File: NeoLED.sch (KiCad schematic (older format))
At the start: 2 parts

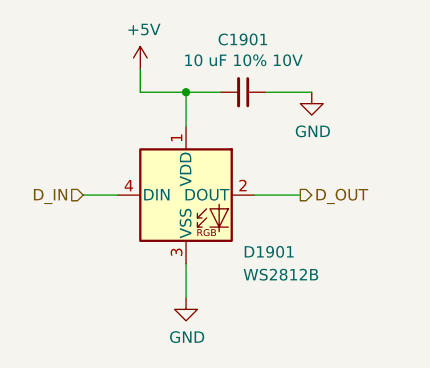
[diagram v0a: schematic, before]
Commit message: Added PCA9745B16B. Updated schematic. ERC Passes.
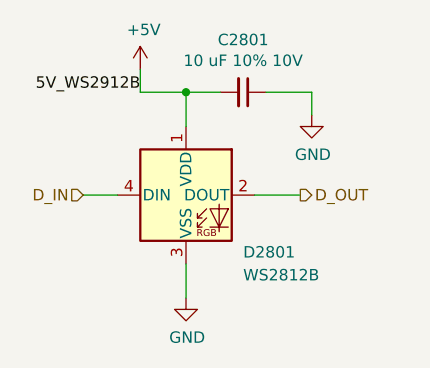
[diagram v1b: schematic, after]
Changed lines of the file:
@@
 AR Path="/61A0B661/61A1D841/61A17A93" Ref="D2701"  Part="1"
 AR Path="/61A0B661/61A1D845/61A17A93" Ref="D2801"  Part="1"
-F 0 "D1901" H 5450 2450 50  0000 L CNN
+F 0 "D2801" H 5450 2450 50  0000 L CNN
 F 1 "WS2812B" H 5450 2350 50  0000 L CNN
 F 2 "LED_SMD:LED_WS2812B_PLCC4_5.0x5.0mm_P3.2mm" H 5250 2400 50  0001 L TNN
@@
 AR Path="/61A0B661/61A1D841/61A18EF9" Ref="#PWR02701"  Part="1"
 AR Path="/61A0B661/61A1D845/61A18EF9" Ref="#PWR02801"  Part="1"
-F 0 "#PWR01901" H 5000 2000 50  0001 C CNN
+F 0 "#PWR02801" H 5000 2000 50  0001 C CNN
 F 1 "+5V" H 5015 2323 50  0000 C CNN
 F 2 "" H 5000 2150 50  0001 C CNN
@@
 AR Path="/61A0B661/61A1D841/61A198EA" Ref="C2701"  Part="1"
 AR Path="/61A0B661/61A1D845/61A198EA" Ref="C2801"  Part="1"
-F 0 "C1901" V 5221 2250 50  0000 C CNN
+F 0 "C2801" V 5221 2250 50  0000 C CNN
 F 1 "10 uF 10% 10V" V 5312 2250 50  0000 C CNN
 F 2 "Capacitor_SMD:C_0805_2012Metric_Pad1.18x1.45mm_HandSolder" H 5450 2250 50  0001 C CNN
@@
 AR Path="/61A0B661/61A1D841/61A1B1AB" Ref="#PWR02702"  Part="1"
 AR Path="/61A0B661/61A1D845/61A1B1AB" Ref="#PWR02802"  Part="1"
-F 0 "#PWR01902" H 5200 2900 50  0001 C CNN
+F 0 "#PWR02802" H 5200 2900 50  0001 C CNN
 F 1 "GND" H 5205 2977 50  0000 C CNN
 F 2 "" H 5200 3150 50  0001 C CNN
@@
 L power:GND #PWR01903
 U 1 1 61A1B656
-P 5750 2250
+P 5750 2350
 AR Path="/61A0B661/61A171D3/61A1B656" Ref="#PWR01903"  Part="1"
 AR Path="/61A0B661/61A1CCBC/61A1B656" Ref="#PWR02003"  Part="1"
@@
 AR Path="/61A0B661/61A1D841/61A1B656" Ref="#PWR02703"  Part="1"
 AR Path="/61A0B661/61A1D845/61A1B656" Ref="#PWR02803"  Part="1"
-F 0 "#PWR01903" H 5750 2000 50  0001 C CNN
-F 1 "GND" H 5755 2077 50  0000 C CNN
-F 2 "" H 5750 2250 50  0001 C CNN
-F 3 "" H 5750 2250 50  0001 C CNN
-	1    5750 2250
+F 0 "#PWR02803" H 5750 2100 50  0001 C CNN
+F 1 "GND" H 5755 2177 50  0000 C CNN
+F 2 "" H 5750 2350 50  0001 C CNN
+F 3 "" H 5750 2350 50  0001 C CNN
+	1    5750 2350
 	1    0    0    -1
 $EndComp
@@
 	5000 2250 5000 2150
 Connection ~ 5200 2250
+Text Label 5000 2250 2    50   ~ 0
+5V_WS2912B
+Wire Wire Line
+	5750 2250 5750 2350
 $EndSCHEMATC

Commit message: fixed broken schematics becuase of deleted rescue files. ECA passes.
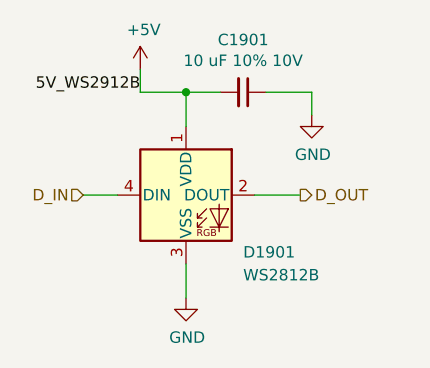
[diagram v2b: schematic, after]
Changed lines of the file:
@@
 AR Path="/61A0B661/61A1D841/61A17A93" Ref="D2701"  Part="1"
 AR Path="/61A0B661/61A1D845/61A17A93" Ref="D2801"  Part="1"
-F 0 "D2801" H 5450 2450 50  0000 L CNN
+F 0 "D1901" H 5450 2450 50  0000 L CNN
 F 1 "WS2812B" H 5450 2350 50  0000 L CNN
 F 2 "LED_SMD:LED_WS2812B_PLCC4_5.0x5.0mm_P3.2mm" H 5250 2400 50  0001 L TNN
@@
 AR Path="/61A0B661/61A1D841/61A198EA" Ref="C2701"  Part="1"
 AR Path="/61A0B661/61A1D845/61A198EA" Ref="C2801"  Part="1"
-F 0 "C2801" V 5221 2250 50  0000 C CNN
+F 0 "C1901" V 5221 2250 50  0000 C CNN
 F 1 "10 uF 10% 10V" V 5312 2250 50  0000 C CNN
 F 2 "Capacitor_SMD:C_0805_2012Metric_Pad1.18x1.45mm_HandSolder" H 5450 2250 50  0001 C CNN

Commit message: initial layout
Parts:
- renumbered C1901 to C1701, D1901 to D1701
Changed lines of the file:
@@
 $Descr A4 11693 8268
 encoding utf-8
-Sheet 17 29
+Sheet 18 29
 Title ""
 Date ""
@@
 $EndDescr
 $Comp
-L TMPCB_R2:WS2812B D1901
+L TMPCB_R2:WS2812B D1701
 U 1 1 61A17A93
 P 5200 2700
-AR Path="/61A0B661/61A171D3/61A17A93" Ref="D1901"  Part="1"
-AR Path="/61A0B661/61A1CCBC/61A17A93" Ref="D2001"  Part="1"
-AR Path="/61A0B661/61A1CE5F/61A17A93" Ref="D2101"  Part="1"
-AR Path="/61A0B661/61A1D175/61A17A93" Ref="D2201"  Part="1"
-AR Path="/61A0B661/61A1D179/61A17A93" Ref="D2301"  Part="1"
-AR Path="/61A0B661/61A1D17D/61A17A93" Ref="D2401"  Part="1"
-AR Path="/61A0B661/61A1D839/61A17A93" Ref="D2501"  Part="1"
-AR Path="/61A0B661/61A1D83D/61A17A93" Ref="D2601"  Part="1"
-AR Path="/61A0B661/61A1D841/61A17A93" Ref="D2701"  Part="1"
-AR Path="/61A0B661/61A1D845/61A17A93" Ref="D2801"  Part="1"
-F 0 "D1901" H 5450 2450 50  0000 L CNN
+AR Path="/61A0B661/61A171D3/61A17A93" Ref="D1701"  Part="1"
+AR Path="/61A0B661/61A1CCBC/61A17A93" Ref="D1801"  Part="1"
+AR Path="/61A0B661/61A1CE5F/61A17A93" Ref="D1901"  Part="1"
+AR Path="/61A0B661/61A1D175/61A17A93" Ref="D2001"  Part="1"
+AR Path="/61A0B661/61A1D179/61A17A93" Ref="D2101"  Part="1"
+AR Path="/61A0B661/61A1D17D/61A17A93" Ref="D2201"  Part="1"
+AR Path="/61A0B661/61A1D839/61A17A93" Ref="D2301"  Part="1"
+AR Path="/61A0B661/61A1D83D/61A17A93" Ref="D2401"  Part="1"
+AR Path="/61A0B661/61A1D841/61A17A93" Ref="D2501"  Part="1"
+AR Path="/61A0B661/61A1D845/61A17A93" Ref="D2601"  Part="1"
+F 0 "D1801" H 5450 2450 50  0000 L CNN
 F 1 "WS2812B" H 5450 2350 50  0000 L CNN
 F 2 "LED_SMD:LED_WS2812B_PLCC4_5.0x5.0mm_P3.2mm" H 5250 2400 50  0001 L TNN
@@
 	5200 3150 5200 3000
 $Comp
-L power:+5V #PWR01901
+L power:+5V #PWR01701
 U 1 1 61A18EF9
 P 5000 2150
-AR Path="/61A0B661/61A171D3/61A18EF9" Ref="#PWR01901"  Part="1"
-AR Path="/61A0B661/61A1CCBC/61A18EF9" Ref="#PWR02001"  Part="1"
-AR Path="/61A0B661/61A1CE5F/61A18EF9" Ref="#PWR02101"  Part="1"
-AR Path="/61A0B661/61A1D175/61A18EF9" Ref="#PWR02201"  Part="1"
-AR Path="/61A0B661/61A1D179/61A18EF9" Ref="#PWR02301"  Part="1"
-AR Path="/61A0B661/61A1D17D/61A18EF9" Ref="#PWR02401"  Part="1"
-AR Path="/61A0B661/61A1D839/61A18EF9" Ref="#PWR02501"  Part="1"
-AR Path="/61A0B661/61A1D83D/61A18EF9" Ref="#PWR02601"  Part="1"
-AR Path="/61A0B661/61A1D841/61A18EF9" Ref="#PWR02701"  Part="1"
-AR Path="/61A0B661/61A1D845/61A18EF9" Ref="#PWR02801"  Part="1"
-F 0 "#PWR02801" H 5000 2000 50  0001 C CNN
+AR Path="/61A0B661/61A171D3/61A18EF9" Ref="#PWR01701"  Part="1"
+AR Path="/61A0B661/61A1CCBC/61A18EF9" Ref="#PWR01801"  Part="1"
+AR Path="/61A0B661/61A1CE5F/61A18EF9" Ref="#PWR01901"  Part="1"
+AR Path="/61A0B661/61A1D175/61A18EF9" Ref="#PWR02001"  Part="1"
+AR Path="/61A0B661/61A1D179/61A18EF9" Ref="#PWR02101"  Part="1"
+AR Path="/61A0B661/61A1D17D/61A18EF9" Ref="#PWR02201"  Part="1"
+AR Path="/61A0B661/61A1D839/61A18EF9" Ref="#PWR02301"  Part="1"
+AR Path="/61A0B661/61A1D83D/61A18EF9" Ref="#PWR02401"  Part="1"
+AR Path="/61A0B661/61A1D841/61A18EF9" Ref="#PWR02501"  Part="1"
+AR Path="/61A0B661/61A1D845/61A18EF9" Ref="#PWR02601"  Part="1"
+F 0 "#PWR01801" H 5000 2000 50  0001 C CNN
 F 1 "+5V" H 5015 2323 50  0000 C CNN
 F 2 "" H 5000 2150 50  0001 C CNN
@@
 $EndComp
 $Comp
-L Device:C_Small C1901
+L Device:C_Small C1701
 U 1 1 61A198EA
 P 5450 2250
-AR Path="/61A0B661/61A171D3/61A198EA" Ref="C1901"  Part="1"
-AR Path="/61A0B661/61A1CCBC/61A198EA" Ref="C2001"  Part="1"
-AR Path="/61A0B661/61A1CE5F/61A198EA" Ref="C2101"  Part="1"
-AR Path="/61A0B661/61A1D175/61A198EA" Ref="C2201"  Part="1"
-AR Path="/61A0B661/61A1D179/61A198EA" Ref="C2301"  Part="1"
-AR Path="/61A0B661/61A1D17D/61A198EA" Ref="C2401"  Part="1"
-AR Path="/61A0B661/61A1D839/61A198EA" Ref="C2501"  Part="1"
-AR Path="/61A0B661/61A1D83D/61A198EA" Ref="C2601"  Part="1"
-AR Path="/61A0B661/61A1D841/61A198EA" Ref="C2701"  Part="1"
-AR Path="/61A0B661/61A1D845/61A198EA" Ref="C2801"  Part="1"
-F 0 "C1901" V 5221 2250 50  0000 C CNN
+AR Path="/61A0B661/61A171D3/61A198EA" Ref="C1701"  Part="1"
+AR Path="/61A0B661/61A1CCBC/61A198EA" Ref="C1801"  Part="1"
+AR Path="/61A0B661/61A1CE5F/61A198EA" Ref="C1901"  Part="1"
+AR Path="/61A0B661/61A1D175/61A198EA" Ref="C2001"  Part="1"
+AR Path="/61A0B661/61A1D179/61A198EA" Ref="C2101"  Part="1"
+AR Path="/61A0B661/61A1D17D/61A198EA" Ref="C2201"  Part="1"
+AR Path="/61A0B661/61A1D839/61A198EA" Ref="C2301"  Part="1"
+AR Path="/61A0B661/61A1D83D/61A198EA" Ref="C2401"  Part="1"
+AR Path="/61A0B661/61A1D841/61A198EA" Ref="C2501"  Part="1"
+AR Path="/61A0B661/61A1D845/61A198EA" Ref="C2601"  Part="1"
+F 0 "C1801" V 5221 2250 50  0000 C CNN
 F 1 "10 uF 10% 10V" V 5312 2250 50  0000 C CNN
 F 2 "Capacitor_SMD:C_0805_2012Metric_Pad1.18x1.45mm_HandSolder" H 5450 2250 50  0001 C CNN
@@
 $EndComp
 $Comp
-L power:GND #PWR01902
+L power:GND #PWR01702
 U 1 1 61A1B1AB
 P 5200 3150
-AR Path="/61A0B661/61A171D3/61A1B1AB" Ref="#PWR01902"  Part="1"
-AR Path="/61A0B661/61A1CCBC/61A1B1AB" Ref="#PWR02002"  Part="1"
-AR Path="/61A0B661/61A1CE5F/61A1B1AB" Ref="#PWR02102"  Part="1"
-AR Path="/61A0B661/61A1D175/61A1B1AB" Ref="#PWR02202"  Part="1"
-AR Path="/61A0B661/61A1D179/61A1B1AB" Ref="#PWR02302"  Part="1"
-AR Path="/61A0B661/61A1D17D/61A1B1AB" Ref="#PWR02402"  Part="1"
-AR Path="/61A0B661/61A1D839/61A1B1AB" Ref="#PWR02502"  Part="1"
-AR Path="/61A0B661/61A1D83D/61A1B1AB" Ref="#PWR02602"  Part="1"
-AR Path="/61A0B661/61A1D841/61A1B1AB" Ref="#PWR02702"  Part="1"
-AR Path="/61A0B661/61A1D845/61A1B1AB" Ref="#PWR02802"  Part="1"
-F 0 "#PWR02802" H 5200 2900 50  0001 C CNN
+AR Path="/61A0B661/61A171D3/61A1B1AB" Ref="#PWR01702"  Part="1"
+AR Path="/61A0B661/61A1CCBC/61A1B1AB" Ref="#PWR01802"  Part="1"
+AR Path="/61A0B661/61A1CE5F/61A1B1AB" Ref="#PWR01902"  Part="1"
+AR Path="/61A0B661/61A1D175/61A1B1AB" Ref="#PWR02002"  Part="1"
+AR Path="/61A0B661/61A1D179/61A1B1AB" Ref="#PWR02102"  Part="1"
+AR Path="/61A0B661/61A1D17D/61A1B1AB" Ref="#PWR02202"  Part="1"
+AR Path="/61A0B661/61A1D839/61A1B1AB" Ref="#PWR02302"  Part="1"
+AR Path="/61A0B661/61A1D83D/61A1B1AB" Ref="#PWR02402"  Part="1"
+AR Path="/61A0B661/61A1D841/61A1B1AB" Ref="#PWR02502"  Part="1"
+AR Path="/61A0B661/61A1D845/61A1B1AB" Ref="#PWR02602"  Part="1"
+F 0 "#PWR01802" H 5200 2900 50  0001 C CNN
 F 1 "GND" H 5205 2977 50  0000 C CNN
 F 2 "" H 5200 3150 50  0001 C CNN
@@
 $EndComp
 $Comp
-L power:GND #PWR01903
+L power:GND #PWR01703
 U 1 1 61A1B656
 P 5750 2350
-AR Path="/61A0B661/61A171D3/61A1B656" Ref="#PWR01903"  Part="1"
-AR Path="/61A0B661/61A1CCBC/61A1B656" Ref="#PWR02003"  Part="1"
-AR Path="/61A0B661/61A1CE5F/61A1B656" Ref="#PWR02103"  Part="1"
-AR Path="/61A0B661/61A1D175/61A1B656" Ref="#PWR02203"  Part="1"
-AR Path="/61A0B661/61A1D179/61A1B656" Ref="#PWR02303"  Part="1"
-AR Path="/61A0B661/61A1D17D/61A1B656" Ref="#PWR02403"  Part="1"
-AR Path="/61A0B661/61A1D839/61A1B656" Ref="#PWR02503"  Part="1"
-AR Path="/61A0B661/61A1D83D/61A1B656" Ref="#PWR02603"  Part="1"
-AR Path="/61A0B661/61A1D841/61A1B656" Ref="#PWR02703"  Part="1"
-AR Path="/61A0B661/61A1D845/61A1B656" Ref="#PWR02803"  Part="1"
-F 0 "#PWR02803" H 5750 2100 50  0001 C CNN
+AR Path="/61A0B661/61A171D3/61A1B656" Ref="#PWR01703"  Part="1"
+AR Path="/61A0B661/61A1CCBC/61A1B656" Ref="#PWR01803"  Part="1"
+AR Path="/61A0B661/61A1CE5F/61A1B656" Ref="#PWR01903"  Part="1"
+AR Path="/61A0B661/61A1D175/61A1B656" Ref="#PWR02003"  Part="1"
+AR Path="/61A0B661/61A1D179/61A1B656" Ref="#PWR02103"  Part="1"
+AR Path="/61A0B661/61A1D17D/61A1B656" Ref="#PWR02203"  Part="1"
+AR Path="/61A0B661/61A1D839/61A1B656" Ref="#PWR02303"  Part="1"
+AR Path="/61A0B661/61A1D83D/61A1B656" Ref="#PWR02403"  Part="1"
+AR Path="/61A0B661/61A1D841/61A1B656" Ref="#PWR02503"  Part="1"
+AR Path="/61A0B661/61A1D845/61A1B656" Ref="#PWR02603"  Part="1"
+F 0 "#PWR01803" H 5750 2100 50  0001 C CNN
 F 1 "GND" H 5755 2177 50  0000 C CNN
 F 2 "" H 5750 2350 50  0001 C CNN

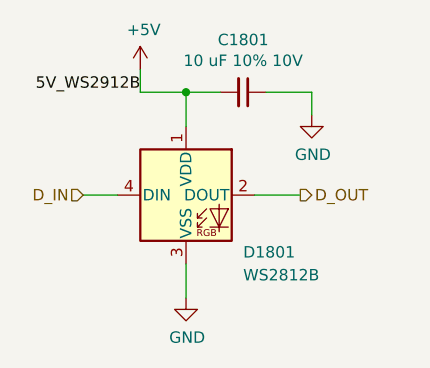
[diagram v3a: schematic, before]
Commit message: Switch NeoPixel to SK6812MINI-E
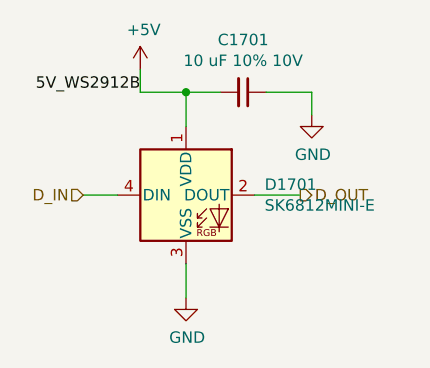
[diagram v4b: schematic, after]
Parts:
- removed D1701: WS2812B, LED_SMD:LED_WS2812B_PLCC4_5.0x5.0mm_P3.2mm, symbol TMPCB_R2:WS2812B
- added D1701: SK6812MINI-E, Macro Keyboard:MX_SK6812MINI-E, symbol Macro_Keyboard:SK6812MINI-E
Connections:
- net +5V: now also D1701.1 (VDD)
- net D_IN: now also D1701.4 (DIN)
- net D_OUT: now also D1701.2 (DOUT)
- net GND: now also D1701.3 (VSS)
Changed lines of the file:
@@
 $Descr A4 11693 8268
 encoding utf-8
-Sheet 18 29
+Sheet 17 29
 Title ""
 Date ""
@@
 Comment4 ""
 $EndDescr
-$Comp
-L TMPCB_R2:WS2812B D1701
-U 1 1 61A17A93
-P 5200 2700
-AR Path="/61A0B661/61A171D3/61A17A93" Ref="D1701"  Part="1"
-AR Path="/61A0B661/61A1CCBC/61A17A93" Ref="D1801"  Part="1"
-AR Path="/61A0B661/61A1CE5F/61A17A93" Ref="D1901"  Part="1"
-AR Path="/61A0B661/61A1D175/61A17A93" Ref="D2001"  Part="1"
-AR Path="/61A0B661/61A1D179/61A17A93" Ref="D2101"  Part="1"
-AR Path="/61A0B661/61A1D17D/61A17A93" Ref="D2201"  Part="1"
-AR Path="/61A0B661/61A1D839/61A17A93" Ref="D2301"  Part="1"
-AR Path="/61A0B661/61A1D83D/61A17A93" Ref="D2401"  Part="1"
-AR Path="/61A0B661/61A1D841/61A17A93" Ref="D2501"  Part="1"
-AR Path="/61A0B661/61A1D845/61A17A93" Ref="D2601"  Part="1"
-F 0 "D1801" H 5450 2450 50  0000 L CNN
-F 1 "WS2812B" H 5450 2350 50  0000 L CNN
-F 2 "LED_SMD:LED_WS2812B_PLCC4_5.0x5.0mm_P3.2mm" H 5250 2400 50  0001 L TNN
-F 3 "http://cdn.sparkfun.com/datasheets/BreakoutBoards/WS2812B.pdf" H 5300 2325 50  0001 L TNN
-F 4 "1568-COM-16347CT-ND" H 5200 2700 50  0001 C CNN "Digikey PN"
-F 5 "SparkFun Electronics" H 5200 2700 50  0001 C CNN "MFG"
-F 6 "COM-16347" H 5200 2700 50  0001 C CNN "MFG #"
-	1    5200 2700
-	1    0    0    -1
-$EndComp
 Text HLabel 4750 2700 0    50   Input ~ 0
 D_IN
@@
 AR Path="/61A0B661/61A1D841/61A18EF9" Ref="#PWR02501"  Part="1"
 AR Path="/61A0B661/61A1D845/61A18EF9" Ref="#PWR02601"  Part="1"
-F 0 "#PWR01801" H 5000 2000 50  0001 C CNN
+F 0 "#PWR01701" H 5000 2000 50  0001 C CNN
 F 1 "+5V" H 5015 2323 50  0000 C CNN
 F 2 "" H 5000 2150 50  0001 C CNN
@@
 AR Path="/61A0B661/61A1D841/61A198EA" Ref="C2501"  Part="1"
 AR Path="/61A0B661/61A1D845/61A198EA" Ref="C2601"  Part="1"
-F 0 "C1801" V 5221 2250 50  0000 C CNN
+F 0 "C1701" V 5221 2250 50  0000 C CNN
 F 1 "10 uF 10% 10V" V 5312 2250 50  0000 C CNN
 F 2 "Capacitor_SMD:C_0805_2012Metric_Pad1.18x1.45mm_HandSolder" H 5450 2250 50  0001 C CNN
@@
 AR Path="/61A0B661/61A1D841/61A1B1AB" Ref="#PWR02502"  Part="1"
 AR Path="/61A0B661/61A1D845/61A1B1AB" Ref="#PWR02602"  Part="1"
-F 0 "#PWR01802" H 5200 2900 50  0001 C CNN
+F 0 "#PWR01702" H 5200 2900 50  0001 C CNN
 F 1 "GND" H 5205 2977 50  0000 C CNN
 F 2 "" H 5200 3150 50  0001 C CNN
@@
 AR Path="/61A0B661/61A1D841/61A1B656" Ref="#PWR02503"  Part="1"
 AR Path="/61A0B661/61A1D845/61A1B656" Ref="#PWR02603"  Part="1"
-F 0 "#PWR01803" H 5750 2100 50  0001 C CNN
+F 0 "#PWR01703" H 5750 2100 50  0001 C CNN
 F 1 "GND" H 5755 2177 50  0000 C CNN
 F 2 "" H 5750 2350 50  0001 C CNN
@@
 Wire Wire Line
 	5750 2250 5750 2350
+$Comp
+L Macro_Keyboard:SK6812MINI-E D1701
+U 1 1 61A46C26
+P 5200 2700
+AR Path="/61A0B661/61A171D3/61A46C26" Ref="D1701"  Part="1"
+AR Path="/61A0B661/61A1CCBC/61A46C26" Ref="D1801"  Part="1"
+AR Path="/61A0B661/61A1CE5F/61A46C26" Ref="D1901"  Part="1"
+AR Path="/61A0B661/61A1D175/61A46C26" Ref="D2001"  Part="1"
+AR Path="/61A0B661/61A1D179/61A46C26" Ref="D2101"  Part="1"
+AR Path="/61A0B661/61A1D17D/61A46C26" Ref="D2201"  Part="1"
+AR Path="/61A0B661/61A1D839/61A46C26" Ref="D2301"  Part="1"
+AR Path="/61A0B661/61A1D83D/61A46C26" Ref="D2401"  Part="1"
+AR Path="/61A0B661/61A1D841/61A46C26" Ref="D2501"  Part="1"
+AR Path="/61A0B661/61A1D845/61A46C26" Ref="D2601"  Part="1"
+F 0 "D1701" H 5544 2746 50  0000 L CNN
+F 1 "SK6812MINI-E" H 5544 2655 50  0000 L CNN
+F 2 "Macro Keyboard:MX_SK6812MINI-E" H 5250 2400 50  0001 L TNN
+F 3 "https://cdn-shop.adafruit.com/product-files/4960/4960_SK6812MINI-E_REV02_EN.pdf" H 5300 2325 50  0001 L TNN
+F 4 "1528-4960-ND" H 5200 2700 50  0001 C CNN "Digikey PN"
+F 5 "Adafruit Industries LLC" H 5200 2700 50  0001 C CNN "MFG"
+F 6 "4960" H 5200 2700 50  0001 C CNN "MFG #"
+	1    5200 2700
+	1    0    0    -1
+$EndComp
 $EndSCHEMATC

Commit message: Starting routing
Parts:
- D1701: footprint Macro Keyboard:MX_SK6812MINI-E -> Macro Keyboard:MX_SK6812MINI-E_REV
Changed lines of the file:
@@
 $Descr A4 11693 8268
 encoding utf-8
-Sheet 17 29
+Sheet 18 30
 Title ""
 Date ""
@@
 AR Path="/61A0B661/61A1D841/61A18EF9" Ref="#PWR02501"  Part="1"
 AR Path="/61A0B661/61A1D845/61A18EF9" Ref="#PWR02601"  Part="1"
-F 0 "#PWR01701" H 5000 2000 50  0001 C CNN
+F 0 "#PWR01801" H 5000 2000 50  0001 C CNN
 F 1 "+5V" H 5015 2323 50  0000 C CNN
 F 2 "" H 5000 2150 50  0001 C CNN
@@
 AR Path="/61A0B661/61A1D841/61A198EA" Ref="C2501"  Part="1"
 AR Path="/61A0B661/61A1D845/61A198EA" Ref="C2601"  Part="1"
-F 0 "C1701" V 5221 2250 50  0000 C CNN
+F 0 "C1801" V 5221 2250 50  0000 C CNN
 F 1 "10 uF 10% 10V" V 5312 2250 50  0000 C CNN
 F 2 "Capacitor_SMD:C_0805_2012Metric_Pad1.18x1.45mm_HandSolder" H 5450 2250 50  0001 C CNN
@@
 AR Path="/61A0B661/61A1D841/61A1B1AB" Ref="#PWR02502"  Part="1"
 AR Path="/61A0B661/61A1D845/61A1B1AB" Ref="#PWR02602"  Part="1"
-F 0 "#PWR01702" H 5200 2900 50  0001 C CNN
+F 0 "#PWR01802" H 5200 2900 50  0001 C CNN
 F 1 "GND" H 5205 2977 50  0000 C CNN
 F 2 "" H 5200 3150 50  0001 C CNN
@@
 AR Path="/61A0B661/61A1D841/61A1B656" Ref="#PWR02503"  Part="1"
 AR Path="/61A0B661/61A1D845/61A1B656" Ref="#PWR02603"  Part="1"
-F 0 "#PWR01703" H 5750 2100 50  0001 C CNN
+F 0 "#PWR01803" H 5750 2100 50  0001 C CNN
 F 1 "GND" H 5755 2177 50  0000 C CNN
 F 2 "" H 5750 2350 50  0001 C CNN
@@
 AR Path="/61A0B661/61A1D841/61A46C26" Ref="D2501"  Part="1"
 AR Path="/61A0B661/61A1D845/61A46C26" Ref="D2601"  Part="1"
-F 0 "D1701" H 5544 2746 50  0000 L CNN
+F 0 "D1801" H 5544 2746 50  0000 L CNN
 F 1 "SK6812MINI-E" H 5544 2655 50  0000 L CNN
-F 2 "Macro Keyboard:MX_SK6812MINI-E" H 5250 2400 50  0001 L TNN
+F 2 "Macro Keyboard:MX_SK6812MINI-E_REV" H 5250 2400 50  0001 L TNN
 F 3 "https://cdn-shop.adafruit.com/product-files/4960/4960_SK6812MINI-E_REV02_EN.pdf" H 5300 2325 50  0001 L TNN
 F 4 "1528-4960-ND" H 5200 2700 50  0001 C CNN "Digikey PN"

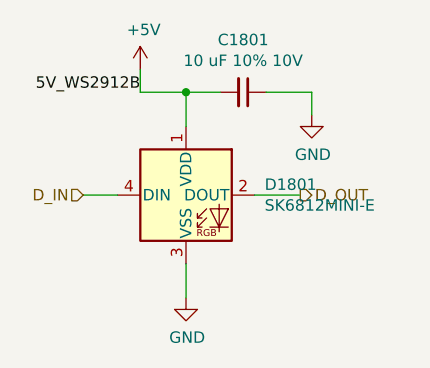
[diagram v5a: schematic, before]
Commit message: Layout completed. Design check passes.
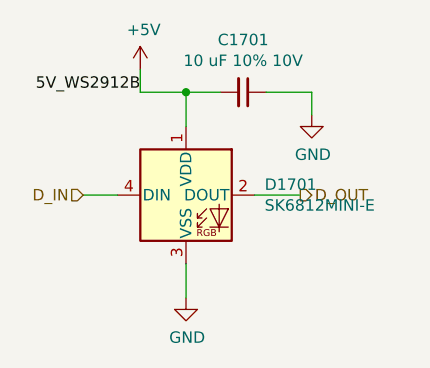
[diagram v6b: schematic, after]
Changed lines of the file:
@@
 $Descr A4 11693 8268
 encoding utf-8
-Sheet 18 30
+Sheet 16 30
 Title ""
 Date ""
@@
 AR Path="/61A0B661/61A1D841/61A18EF9" Ref="#PWR02501"  Part="1"
 AR Path="/61A0B661/61A1D845/61A18EF9" Ref="#PWR02601"  Part="1"
-F 0 "#PWR01801" H 5000 2000 50  0001 C CNN
+F 0 "#PWR01701" H 5000 2000 50  0001 C CNN
 F 1 "+5V" H 5015 2323 50  0000 C CNN
 F 2 "" H 5000 2150 50  0001 C CNN
@@
 AR Path="/61A0B661/61A1D841/61A198EA" Ref="C2501"  Part="1"
 AR Path="/61A0B661/61A1D845/61A198EA" Ref="C2601"  Part="1"
-F 0 "C1801" V 5221 2250 50  0000 C CNN
+F 0 "C1701" V 5221 2250 50  0000 C CNN
 F 1 "10 uF 10% 10V" V 5312 2250 50  0000 C CNN
 F 2 "Capacitor_SMD:C_0805_2012Metric_Pad1.18x1.45mm_HandSolder" H 5450 2250 50  0001 C CNN
@@
 AR Path="/61A0B661/61A1D841/61A1B1AB" Ref="#PWR02502"  Part="1"
 AR Path="/61A0B661/61A1D845/61A1B1AB" Ref="#PWR02602"  Part="1"
-F 0 "#PWR01802" H 5200 2900 50  0001 C CNN
+F 0 "#PWR01702" H 5200 2900 50  0001 C CNN
 F 1 "GND" H 5205 2977 50  0000 C CNN
 F 2 "" H 5200 3150 50  0001 C CNN
@@
 AR Path="/61A0B661/61A1D841/61A1B656" Ref="#PWR02503"  Part="1"
 AR Path="/61A0B661/61A1D845/61A1B656" Ref="#PWR02603"  Part="1"
-F 0 "#PWR01803" H 5750 2100 50  0001 C CNN
+F 0 "#PWR01703" H 5750 2100 50  0001 C CNN
 F 1 "GND" H 5755 2177 50  0000 C CNN
 F 2 "" H 5750 2350 50  0001 C CNN
@@
 AR Path="/61A0B661/61A1D841/61A46C26" Ref="D2501"  Part="1"
 AR Path="/61A0B661/61A1D845/61A46C26" Ref="D2601"  Part="1"
-F 0 "D1801" H 5544 2746 50  0000 L CNN
+F 0 "D1701" H 5544 2746 50  0000 L CNN
 F 1 "SK6812MINI-E" H 5544 2655 50  0000 L CNN
 F 2 "Macro Keyboard:MX_SK6812MINI-E_REV" H 5250 2400 50  0001 L TNN

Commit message: Checkpoint
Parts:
- D1701: Notes (none) -> Comes in pack of 10
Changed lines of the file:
@@
 F 5 "Adafruit Industries LLC" H 5200 2700 50  0001 C CNN "MFG"
 F 6 "4960" H 5200 2700 50  0001 C CNN "MFG #"
+F 7 "Comes in pack of 10" H 5200 2700 50  0001 C CNN "Notes"
 	1    5200 2700
 	1    0    0    -1
